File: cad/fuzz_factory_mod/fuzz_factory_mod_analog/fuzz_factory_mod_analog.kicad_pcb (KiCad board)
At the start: 2 copper layers, 97 parts, among them J101 Conn_01x10_Male, J102 Conn_01x10_Male, Q201 Q_NJFET_DSG, Q202 DMMT3904W, Q203 DMMT3906W, Q204 DMMT3906W, Q401 Q_NJFET_DSG, U301 MC33202, U501 MC33202

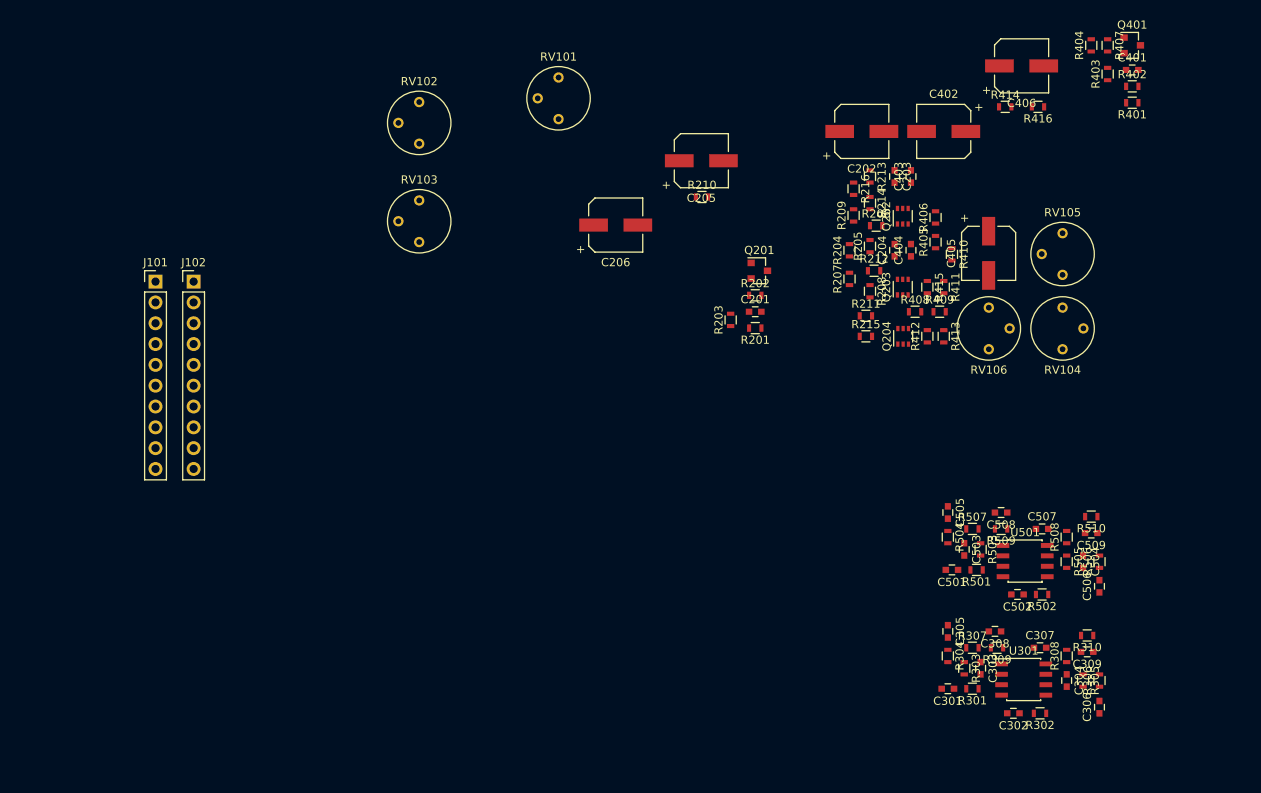
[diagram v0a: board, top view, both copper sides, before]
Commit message: Updated trimmers footprint.
Continued layout.
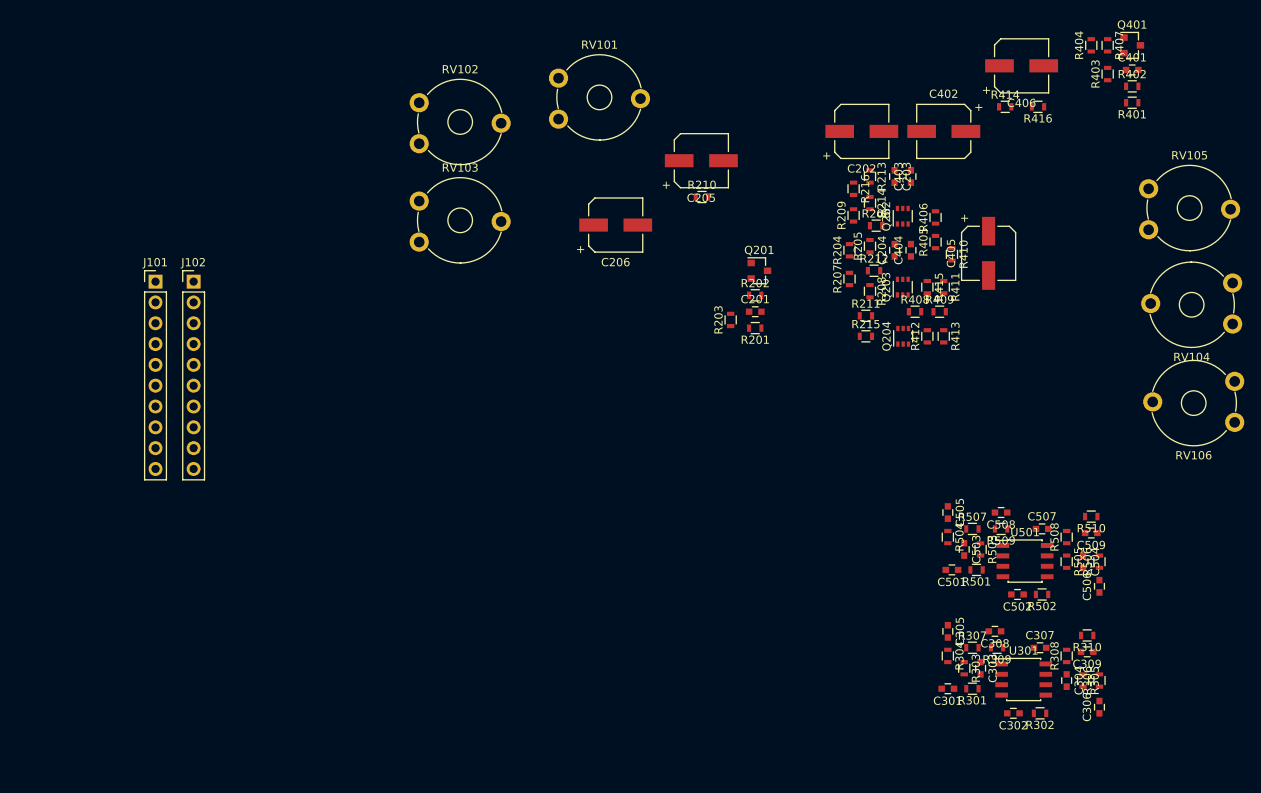
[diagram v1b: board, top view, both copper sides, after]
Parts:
- RV101, RV102, RV103, RV104, RV105, RV106: footprint Potentiometers:Potentiometer_Trimmer_Bourns_3339P_Horizontal -> Potentiometers:Potentiometer_Trimmer_Piher_PT-10v10_Horizontal_Px10.0mm_Py5.0mm
- moved RV106 31.3 mm to (221.5, 83.5)
- moved RV104 21.0 mm to (221.2, 71.5)
- moved RV105 11.9 mm to (211.0, 65.0)

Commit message: Continued layout.
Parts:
- moved J102 42.4 mm to (116.5, 107.5)
- moved J101 39.1 mm to (75.0, 107.5)
